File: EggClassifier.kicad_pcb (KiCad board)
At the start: 2 copper layers, 100 x 100 mm, 54 parts, among them J1 Left_02x24, J10 LCD_CHAR, J11 SERVO2, J12 BME280, J13 UART1, J14 FAN, J15 UART2, J16 AS7265X, J17 TFT_SPI, J2 Right Header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

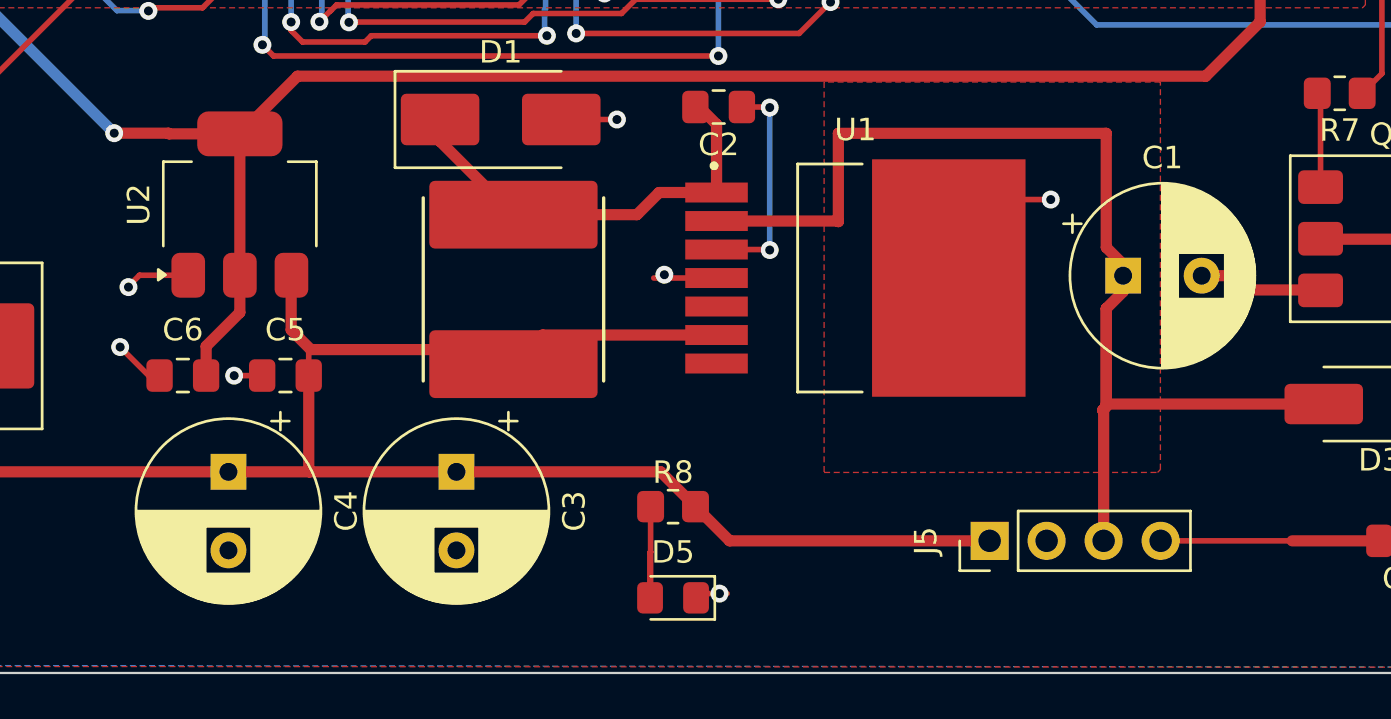
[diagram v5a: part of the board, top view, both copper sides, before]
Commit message: Add footprints to project library
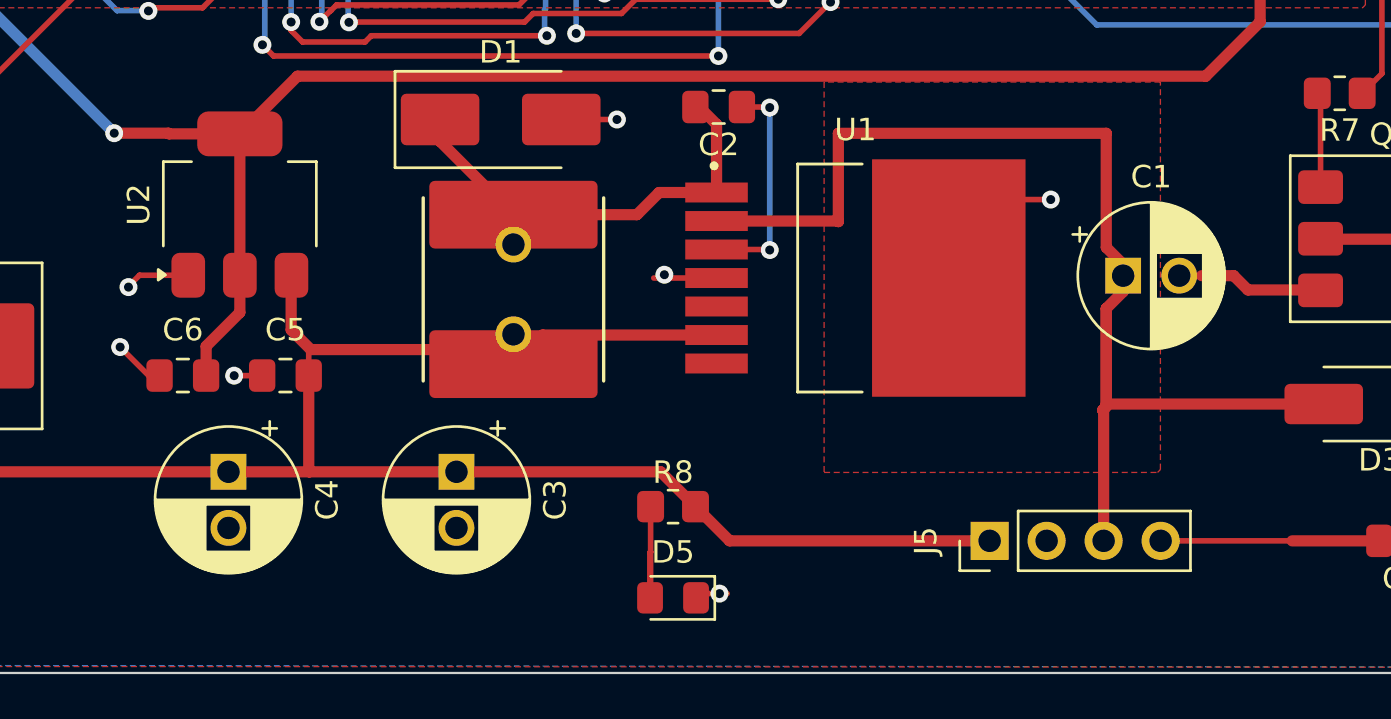
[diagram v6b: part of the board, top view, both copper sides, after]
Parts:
- C1, C3, C4: footprint Capacitor_THT:CP_Radial_D8.0mm_P3.50mm -> EggClassifier:CP_Radial_D6.3mm_P2.50mm_Hole1.0mm
- C10, C11, C2, C5, C6, C7, C8, C9: footprint Capacitor_SMD:C_0805_2012Metric_Pad1.18x1.45mm_HandSolder -> EggClassifier:C_0805_2012Metric_Pad1.18x1.45mm_HandSolder
- D1: footprint Diode_SMD:D_SMB_Handsoldering -> EggClassifier:D_SMB_Handsoldering
- D2, D3, D4: footprint Diode_SMD:D_SMA_Handsoldering -> EggClassifier:D_SMA_Handsoldering
- D5: footprint LED_SMD:LED_0805_2012Metric_Pad1.15x1.40mm_HandSolder -> EggClassifier:LED_0805_2012Metric_Pad1.15x1.40mm_HandSolder
- H1, H2, H3, H4: footprint PCM_JLCPCB:Hole, 3mm -> EggClassifier:Hole, 3mm
- J1, J3: footprint Connector_PinHeader_2.54mm:PinHeader_2x24_P2.54mm_Vertical -> EggClassifier:PinHeader_2x24_P2.54mm_Vertical
- J10, J12, J16, J5: footprint Connector_PinHeader_2.54mm:PinHeader_1x04_P2.54mm_Vertical -> EggClassifier:PinHeader_1x04_P2.54mm_Vertical
- J11, J13, J14, J15, J8, J9: footprint Connector_PinHeader_2.54mm:PinHeader_1x03_P2.54mm_Vertical -> EggClassifier:PinHeader_1x03_P2.54mm_Vertical
- J17: footprint Connector_PinHeader_2.54mm:PinHeader_1x15_P2.54mm_Vertical -> EggClassifier:PinHeader_1x15_P2.54mm_Vertical
- J2, J4: footprint Connector_PinHeader_2.54mm:PinHeader_2x22_P2.54mm_Vertical -> EggClassifier:PinHeader_2x22_P2.54mm_Vertical
- J6: footprint Connector_PinHeader_2.54mm:PinHeader_2x09_P2.54mm_Vertical -> EggClassifier:PinHeader_2x09_P2.54mm_Vertical
- J7: footprint Connector_PinHeader_2.54mm:PinHeader_2x05_P2.54mm_Vertical -> EggClassifier:PinHeader_2x05_P2.54mm_Vertical
- L1: footprint JLCPCB:L_SMD,8x8mm -> EggClassifier:L_SMD,8x8mm
- Q1, Q2, Q3: footprint PCM_Package_TO_SOT_SMD_AKL:SOT-223-3_TabPin2 -> EggClassifier:SOT-223-3_TabPin2
- R1, R10, R11, R2, R3, R4, R5, R6, R7, R8, R9: footprint Resistor_SMD:R_0805_2012Metric_Pad1.20x1.40mm_HandSolder -> EggClassifier:R_0805_2012Metric_Pad1.20x1.40mm_HandSolder
- U1: footprint LM2676S-3.3_NOPB:TO127P1435X464-8N -> EggClassifier:TO127P1435X464-8N
- U2: footprint Package_TO_SOT_SMD:SOT-223-3_TabPin2 -> EggClassifier:SOT-223-3_TabPin2

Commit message: update footprints
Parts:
- C1, C3, C4: footprint EggClassifier:CP_Radial_D6.3mm_P2.50mm_Hole1.0mm -> EggClassifier:CP_Radial_D8.0mm_P3.50mm_Hole1.0mm
